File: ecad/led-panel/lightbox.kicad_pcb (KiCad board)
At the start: 2 copper layers, 127 x 82 mm, 70 parts, among them P1 USB_C_Plug_USB2.0, SW1 RST, SW2 BOOT, SW3 USER1, SW4 USER2, U1 ESP32-S3-WROOM-1, U2 AMS1117-3.3, U3 SN74LVC1T45DBV

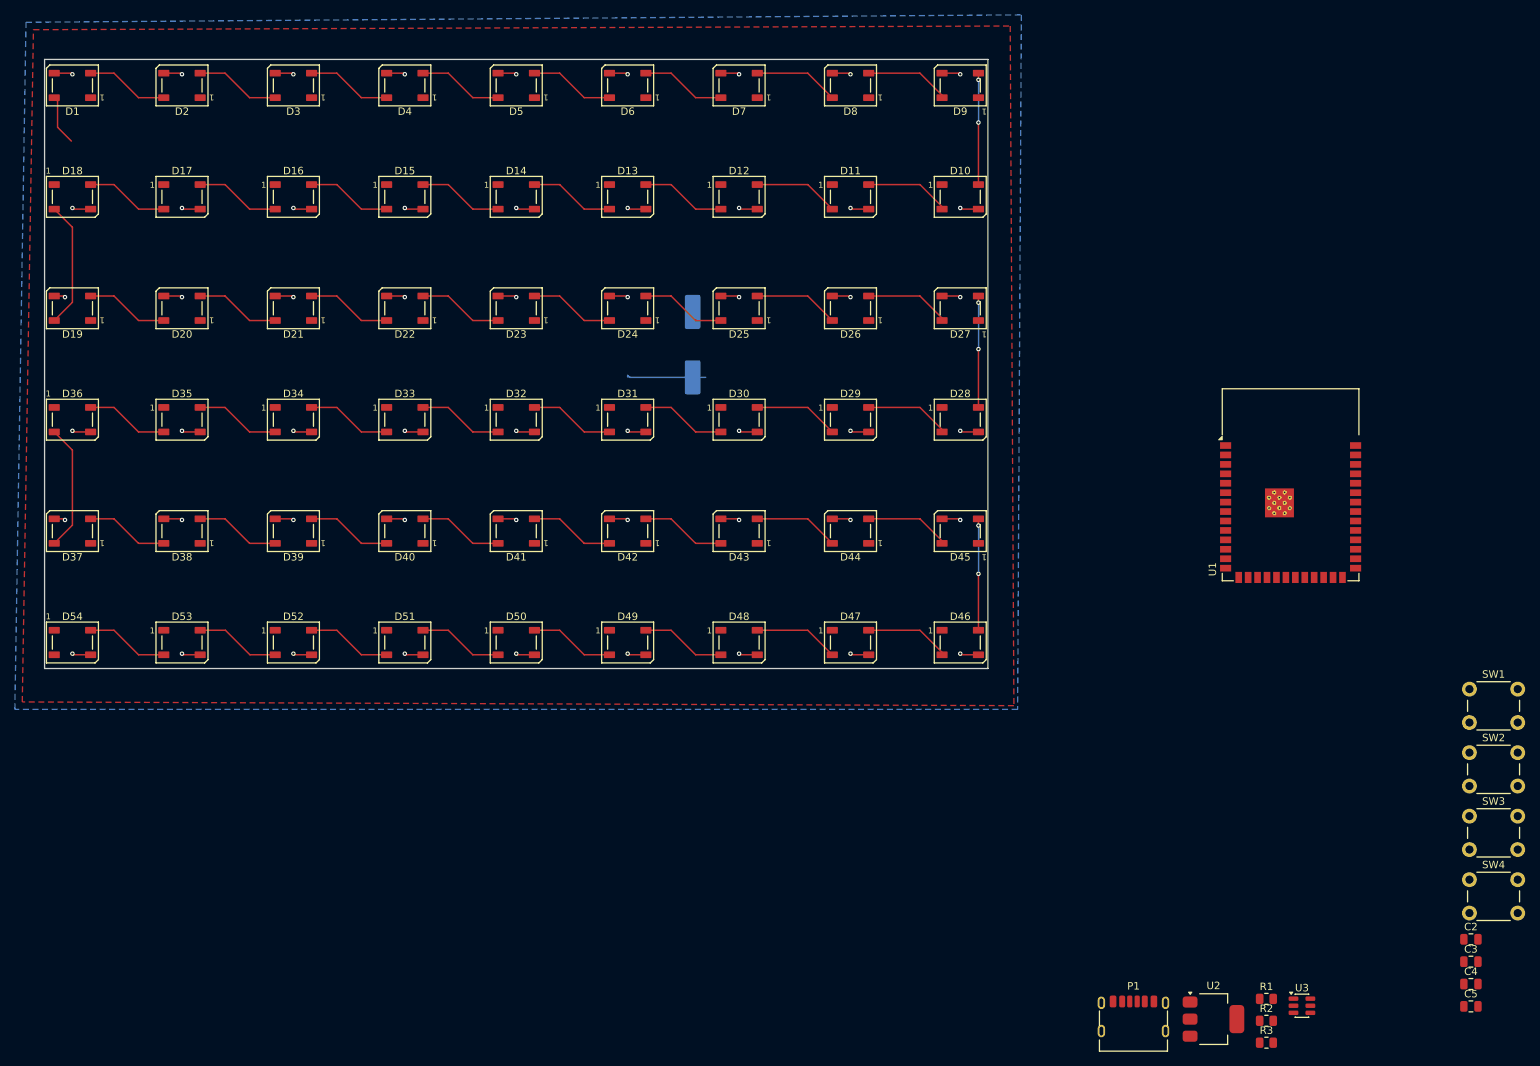
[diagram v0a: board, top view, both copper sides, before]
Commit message: remove USB C port, using JST-XH connector to breakout board instead; add testpoints; switch from 2 gnd planes to 1 5V plane and 1 gnd plane; prelim routing complete
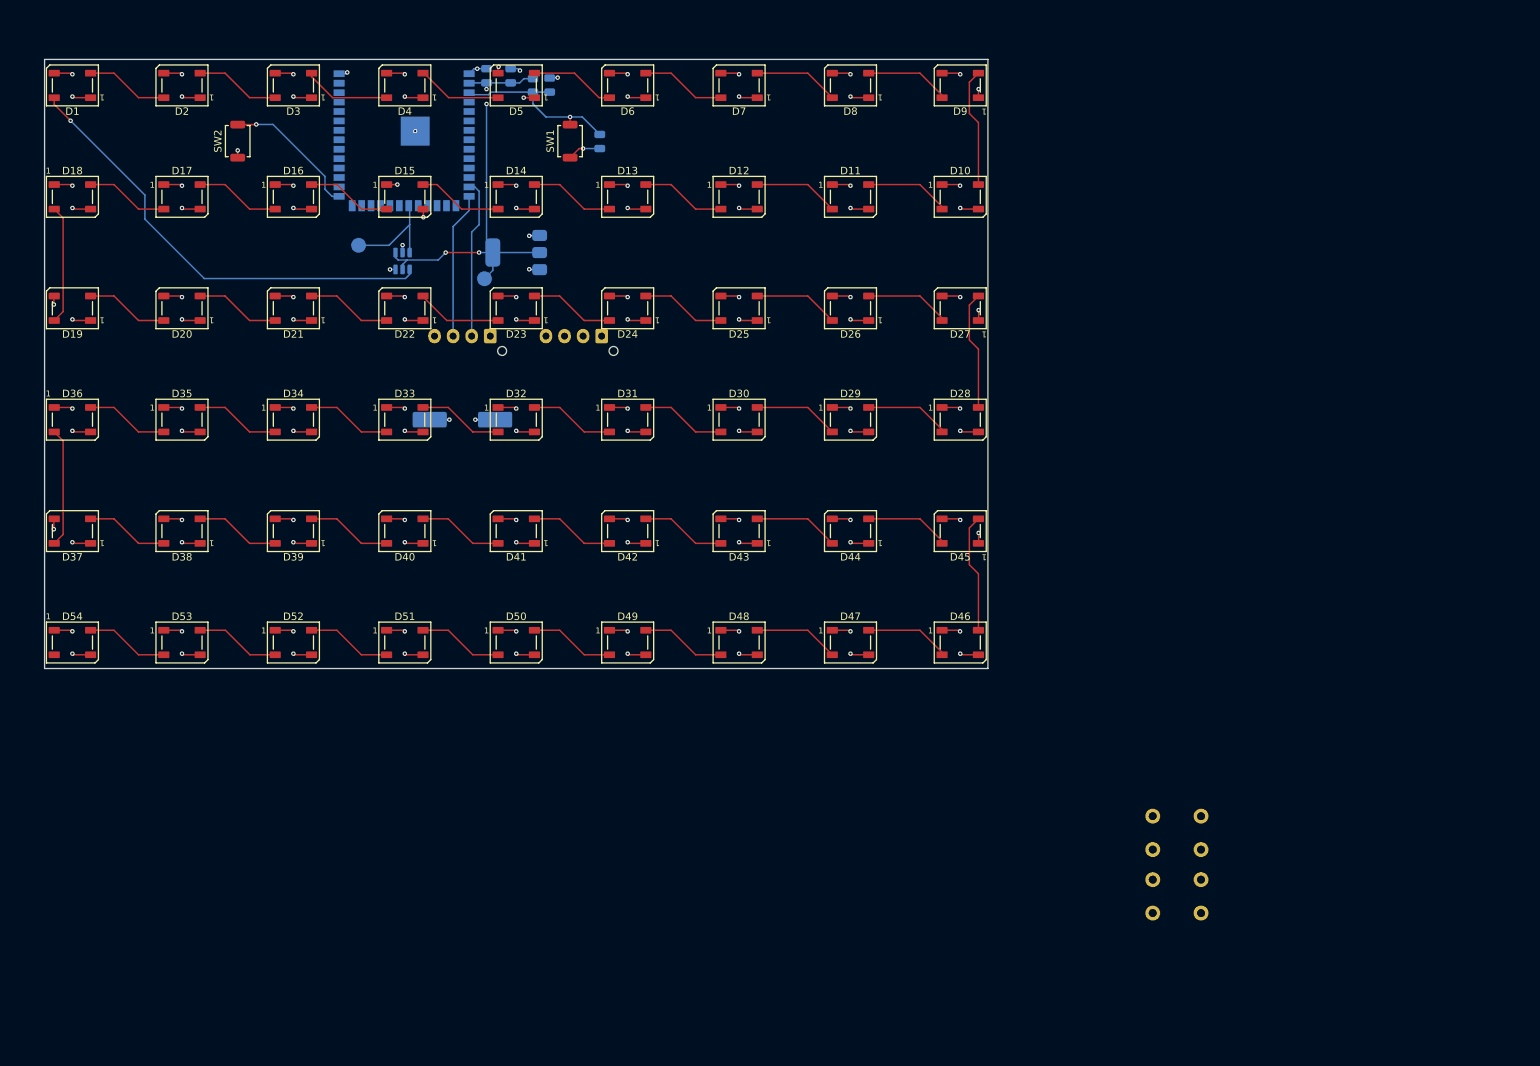
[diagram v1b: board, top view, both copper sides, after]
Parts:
- removed P1: USB_C_Plug_USB2.0, Connector_USB:USB_C_Receptacle_HRO_TYPE-C-31-M-17
- removed R2, R3: 5.1k, Resistor_SMD:R_0805_2012Metric
- added 3V3: TestPoint, TestPoint:TestPoint_Pad_D2.0mm, B.Cu at (59.2, 29.5)
- added LED_GPIO1: TestPoint, TestPoint:TestPoint_Pad_D2.0mm, B.Cu at (42.3, 25.0)
- added PRGM1: Conn_01x04, Connector_JST:JST_XH_B4B-XH-AM_1x04_P2.50mm_Vertical, B.Cu at (60.0, 37.2)
- added PWR1: Conn_01x04, Connector_JST:JST_XH_B4B-XH-AM_1x04_P2.50mm_Vertical, B.Cu at (75.0, 37.2)
- C2, C3, C4, C5, R1, SW3, SW4, U1, U2, U3: moved to B.Cu
- SW1, SW2: footprint Button_Switch_THT:SW_PUSH_6mm -> Button_Switch_SMD:SW_SPST_TS-1088-xR020
- moved SW2 185.1 mm to (26.0, 11.0), turned to 90 degrees
- moved C4 180.3 mm to (59.5, 2.20), turned to 90 degrees
- moved C3 175.9 mm to (62.8, 2.20), turned to 90 degrees
- moved C2 169.1 mm to (68.0, 3.45), turned to 90 degrees
- moved C5 165.3 mm to (74.8, 11.1), turned to -90 degrees
- moved R1 157.7 mm to (65.8, 3.50), turned to -90 degrees
- moved U3 157.2 mm to (48.2, 27.1), turned to -90 degrees
- moved SW1 141.8 mm to (70.8, 11.0), turned to 90 degrees
- moved U2 139.5 mm to (63.5, 26.0), turned to 180 degrees
- moved U1 129.4 mm to (48.4, 7.19), turned to 180 degrees
- moved SW3 36.1 mm to (155.7, 101.9), turned to 180 degrees
- moved SW4 36.1 mm to (155.7, 110.4), turned to 180 degrees
- moved C1 32.6 mm to (56.2, 48.5), turned to 180 degrees
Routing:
- net +5V: track 10.8 -> 134.7 mm, vias 0 -> 57
- net +3V3: track 0.00 -> 59.7 mm, vias 0 -> 4
- net /LED_SIG: track 6.81 -> 61.3 mm, vias 0 -> 1
- net /EN: track 0.00 -> 24.9 mm, vias 0 -> 1
- net /D-: track 0.00 -> 21.5 mm
- net /D+: track 0.00 -> 19.7 mm
- net /IO0: track 0.00 -> 18.7 mm, vias 0 -> 1
- net /LED_GPIO: track 0.00 -> 15.0 mm
- net GND: track 133.7 -> 147.1 mm, vias 54 -> 64
- net /led-grid/led-row1/DOUT: track 17.0 -> 16.0 mm
- net /led-grid/led-row3/DOUT: track 17.0 -> 16.0 mm
- net /led-grid/led-row4/DOUT: track 15.0 -> 16.0 mm, vias 2 -> 0
- net /led-grid/led-row/DOUT: track 15.0 -> 16.0 mm, vias 2 -> 0
- net /led-grid/led-row2/DOUT: track 15.0 -> 16.0 mm, vias 2 -> 0
- added copper zone on In1.Cu, net +5V
- added copper zone on In2.Cu, net GND
- removed copper zone on F.Cu, net +5V
- removed copper zone on B.Cu, net GND
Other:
- copper layers 2 -> 4
- board text removed: "+5V"
- board text removed: "GND"

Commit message: before splitting into 2 boards
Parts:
- added IO15: TestPoint, TestPoint:TestPoint_Pad_D1.5mm, B.Cu at (63.0, 11.2)
- added IO16: TestPoint, TestPoint:TestPoint_Pad_D1.5mm, B.Cu at (60.8, 12.5)
- added IO17: TestPoint, TestPoint:TestPoint_Pad_D1.5mm, B.Cu at (63.0, 14.0)
- added IO18: TestPoint, TestPoint:TestPoint_Pad_D1.5mm, B.Cu at (60.8, 15.2)
- added IO38: TestPoint, TestPoint:TestPoint_Pad_D1.5mm, B.Cu at (27.2, 7.25)
- added IO39: TestPoint, TestPoint:TestPoint_Pad_D1.5mm, B.Cu at (25.0, 6.00)
- added IO4: TestPoint, TestPoint:TestPoint_Pad_D1.5mm, B.Cu at (63.0, 5.75)
- added IO40: TestPoint, TestPoint:TestPoint_Pad_D1.5mm, B.Cu at (27.2, 4.50)
- added IO41: TestPoint, TestPoint:TestPoint_Pad_D1.5mm, B.Cu at (25.0, 3.25)
- added IO42: TestPoint, TestPoint:TestPoint_Pad_D1.5mm, B.Cu at (27.2, 1.75)
- added IO5: TestPoint, TestPoint:TestPoint_Pad_D1.5mm, B.Cu at (60.8, 7.00)
- added IO6: TestPoint, TestPoint:TestPoint_Pad_D1.5mm, B.Cu at (63.0, 8.50)
- added IO7: TestPoint, TestPoint:TestPoint_Pad_D1.5mm, B.Cu at (60.8, 9.75)
- added IO8: TestPoint, TestPoint:TestPoint_Pad_D1.5mm, B.Cu at (63.0, 16.8)
- moved 3V3 12.5 mm to (71.2, 26.0)
- moved C5 7.77 mm to (68.0, 7.20)
- moved LED_GPIO1 1.06 mm to (43.0, 24.2)
- moved PRGM1 0.48 mm to (60.0, 37.7)
- moved PWR1 0.48 mm to (75.0, 37.7)
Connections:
- U1 pad 10: unconnected-(U1-IO17-Pad10) -> Net-(U1-IO17)
- U1 pad 11: unconnected-(U1-IO18-Pad11) -> Net-(U1-IO18)
- U1 pad 12: unconnected-(U1-IO8-Pad12) -> Net-(U1-IO8)
- U1 pad 31: unconnected-(U1-IO38-Pad31) -> Net-(U1-IO38)
- U1 pad 32: unconnected-(U1-IO39-Pad32) -> Net-(U1-IO39)
- U1 pad 33: unconnected-(U1-IO40-Pad33) -> Net-(U1-IO40)
- U1 pad 34: unconnected-(U1-IO41-Pad34) -> Net-(U1-IO41)
- U1 pad 35: unconnected-(U1-IO42-Pad35) -> Net-(U1-IO42)
- U1 pad 4: unconnected-(U1-IO4-Pad4) -> Net-(U1-IO4)
- U1 pad 5: unconnected-(U1-IO5-Pad5) -> Net-(U1-IO5)
- U1 pad 6: unconnected-(U1-IO6-Pad6) -> Net-(U1-IO6)
- U1 pad 7: unconnected-(U1-IO7-Pad7) -> Net-(U1-IO7)
- U1 pad 8: unconnected-(U1-IO15-Pad8) -> Net-(U1-IO15)
- U1 pad 9: unconnected-(U1-IO16-Pad9) -> Net-(U1-IO16)
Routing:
- net Net-(U1-IO41): track 0.00 -> 17.3 mm
- net Net-(U1-IO39): track 0.00 -> 17.2 mm
- net Net-(U1-IO42): track 0.00 -> 15.1 mm
- net Net-(U1-IO40): track 0.00 -> 15.0 mm
- net Net-(U1-IO38): track 0.00 -> 14.9 mm
- net /EN: track 24.9 -> 17.2 mm
- net Net-(U1-IO8): track 0.00 -> 6.20 mm
- net Net-(U1-IO17): track 0.00 -> 6.12 mm
- net Net-(U1-IO15): track 0.00 -> 6.03 mm
- net Net-(U1-IO6): track 0.00 -> 5.94 mm
- net Net-(U1-IO4): track 0.00 -> 5.85 mm
- net Net-(U1-IO18): track 0.00 -> 3.86 mm
- net Net-(U1-IO16): track 0.00 -> 3.77 mm
- net +3V3: track 59.7 -> 63.4 mm
- net Net-(U1-IO7): track 0.00 -> 3.72 mm
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
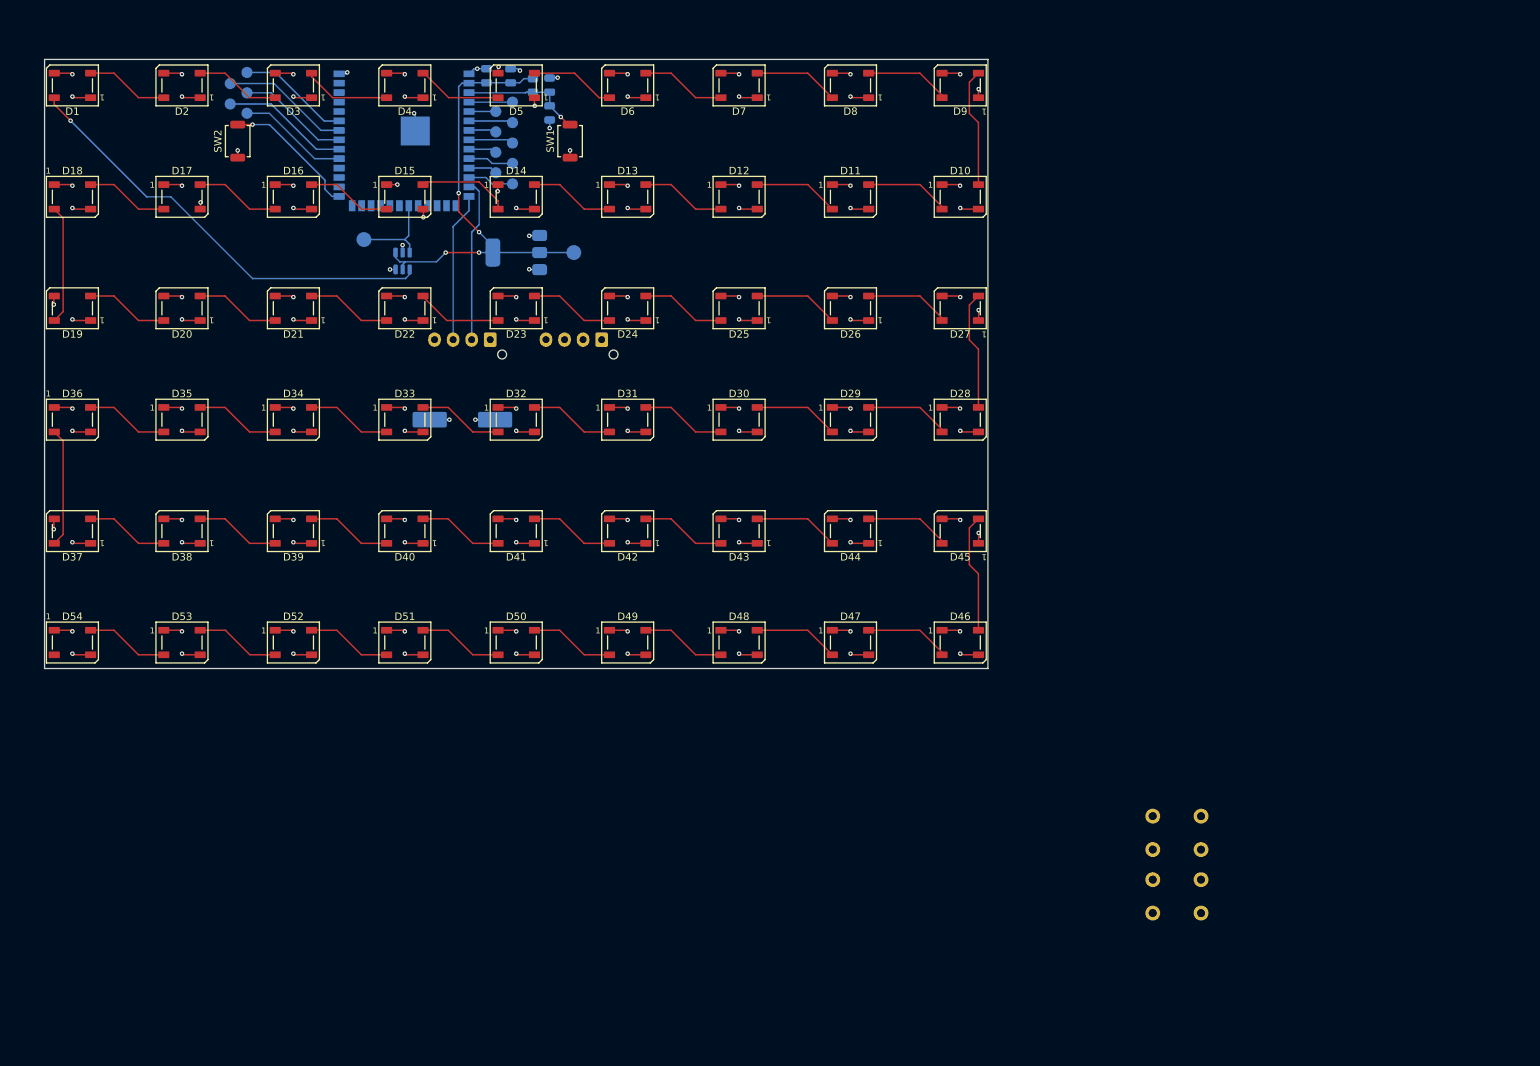
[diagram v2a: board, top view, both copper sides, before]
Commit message: split into 2 boards; switch led panel from 4 layers to 2 layers;
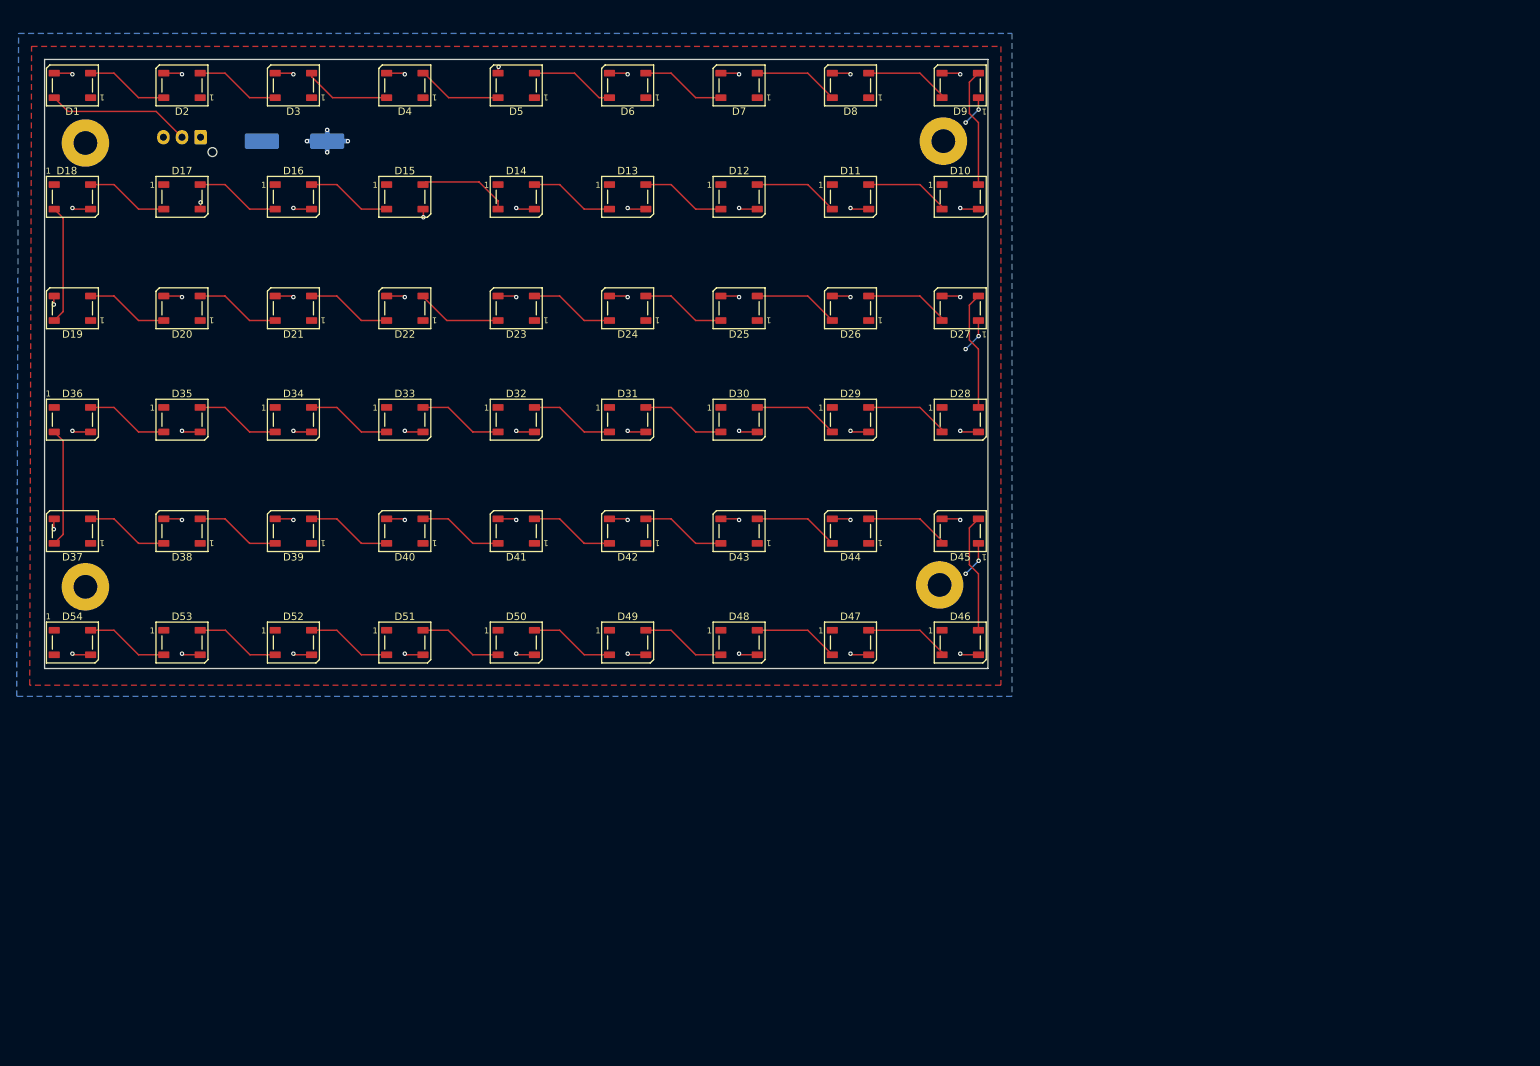
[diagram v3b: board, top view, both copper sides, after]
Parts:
- removed 3V3, LED_GPIO1: TestPoint, TestPoint:TestPoint_Pad_D2.0mm
- removed C2: 1uF, Capacitor_SMD:C_0805_2012Metric
- removed C3: 22uF, Capacitor_SMD:C_0805_2012Metric
- removed C4, C5: 0.1uF, Capacitor_SMD:C_0805_2012Metric
- removed IO15, IO16, IO17, IO18, IO38, IO39, IO4, IO40, IO41, IO42, IO5, IO6, IO7, IO8: TestPoint, TestPoint:TestPoint_Pad_D1.5mm
- removed PRGM1, PWR1: Conn_01x04, Connector_JST:JST_XH_B4B-XH-AM_1x04_P2.50mm_Vertical
- removed R1: 10kΩ, Resistor_SMD:R_0805_2012Metric
- removed SW1: RST, Button_Switch_SMD:SW_SPST_TS-1088-xR020
- removed SW2: BOOT, Button_Switch_SMD:SW_SPST_TS-1088-xR020
- removed SW3: USER1, Button_Switch_THT:SW_PUSH_6mm
- removed SW4: USER2, Button_Switch_THT:SW_PUSH_6mm
- removed U1: ESP32-S3-WROOM-1, RF_Module:ESP32-S3-WROOM-1
- removed U2: AMS1117-3.3, Package_TO_SOT_SMD:SOT-223-3_TabPin2
- removed U3: SN74LVC1T45DBV, Package_TO_SOT_SMD:SOT-23-6
- added H1: MountingHole, MountingHole:MountingHole_3.2mm_M3_Pad, F.Cu at (5.50, 11.2)
- added H2: MountingHole, MountingHole:MountingHole_3.2mm_M3_Pad, F.Cu at (5.50, 71.0)
- added H3: MountingHole, MountingHole:MountingHole_3.2mm_M3_Pad, F.Cu at (121.0, 11.0)
- added H4: MountingHole, MountingHole:MountingHole_3.2mm_M3_Pad, F.Cu at (120.5, 70.8)
- added J1: Conn_01x03, Connector_JST:JST_XH_B3B-XH-AM_1x03_P2.50mm_Vertical, B.Cu at (21.0, 10.5)
- moved C1 43.8 mm to (33.6, 11.0)
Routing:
- net +5V: track 132.8 -> 22.0 mm, vias 57 -> 10
- net +3V3: track 63.4 -> 0.00 mm, vias 4 -> 0
- net /LED_SIG: track 59.4 -> 19.4 mm, vias 1 -> 0
- net /D-: track 22.0 -> 0.00 mm
- net /D+: track 20.2 -> 0.00 mm
- net /IO0: track 18.4 -> 0.00 mm, vias 1 -> 0
- net Net-(U1-IO41): track 17.3 -> 0.00 mm
- net /EN: track 17.2 -> 0.00 mm, vias 1 -> 0
- net Net-(U1-IO39): track 17.2 -> 0.00 mm
- net GND: track 145.5 -> 128.6 mm, vias 65 -> 54
- net Net-(U1-IO42): track 15.1 -> 0.00 mm
- net Net-(U1-IO40): track 15.0 -> 0.00 mm
- net Net-(U1-IO38): track 14.9 -> 0.00 mm
- net /LED_GPIO: track 12.4 -> 0.00 mm
- net Net-(U1-IO8): track 6.20 -> 0.00 mm
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- added copper zone on F.Cu, net +5V
- added copper zone on B.Cu, net GND
- removed copper zone on In1.Cu, net +5V
- removed copper zone on In2.Cu, net GND
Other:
- copper layers 4 -> 2

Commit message: added vertical USB-C connector to controller board; and possibly much more
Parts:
- H1, H2, H3, H4: footprint MountingHole:MountingHole_3.2mm_M3_Pad -> MountingHole:MountingHole_4.3mm_M4_Pad
- moved J1 7.50 mm to (28.5, 10.5)
- moved C1 7.45 mm to (41.1, 11.0)
- moved H1 5.51 mm to (11.0, 11.0)
- moved H2 5.50 mm to (11.0, 71.0)
- moved H3 5.00 mm to (116.0, 11.0)
- moved H4 4.51 mm to (116.0, 71.0)
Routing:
- net /LED_SIG: track 19.4 -> 26.9 mm
- net GND: track 128.6 -> 133.2 mm

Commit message: prelim checks of led panel
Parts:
- H1, H2, H3, H4: footprint MountingHole:MountingHole_4.3mm_M4_Pad -> MountingHole:MountingHole_4.3mm_M4
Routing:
- net +5V: track 22.0 -> 33.0 mm, vias 10 -> 14
- net /LED_SIG: track 26.9 -> 28.1 mm
- net Net-(D14-DOUT): track 12.4 -> 11.8 mm

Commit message: final design review for v1 order; reroute some components; add LED to controller
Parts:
- H1, H2, H3, H4: footprint MountingHole:MountingHole_4.3mm_M4 -> MountingHole:MountingHole_4.3mm_M4_ISO7380_Pad_TopOnly
- moved J1 5.16 mm to (26.0, 15.0), turned to 90 degrees
- moved C1 1.62 mm to (39.5, 10.8), turned to 90 degrees
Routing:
- net +5V: track 33.0 -> 30.9 mm, vias 14 -> 13
- net /LED_SIG: track 28.1 -> 28.9 mm
